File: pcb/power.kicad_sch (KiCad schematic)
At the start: 12 parts, among them U4 LP3993-33B3F

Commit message: Preliminary case design done, moving on to PCB design
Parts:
- removed TP1, TP2, TP3, TP4: ~, TestPoint:TestPoint_Pad_D2.0mm, symbol Connector:TestPoint
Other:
- note removed: "Test points"
- note removed: "label these on PCB"
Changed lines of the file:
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@@
-    (fill (type none))
-  )
-  (rectangle (start 25.4 60.96) (end 57.15 90.17)
-    (stroke (width 0) (type default))
     (fill (type none))
   )
@@
     (effects (font (size 1.5 1.5) (thickness 0.254) bold) (justify left bottom))
   )
-  (text "Test points" (at 26.67 64.77 0)
-    (effects (font (size 1.5 1.5) (thickness 0.254) bold) (justify left bottom))
-  )
   (text "3.3V stepdown" (at 76.2 29.21 0)
     (effects (font (size 1.5 1.5) (thickness 0.254) bold) (justify left bottom))
   )
-  (text "label these on PCB" (at 25.4 91.44 0)
-    (effects (font (size 0.7 0.7) italic (color 108 131 255 1)) (justify left bottom))
-  )
-  (symbol (lib_id "Connector:TestPoint") (at 33.02 72.39 180) (unit 1)
-    (in_bom yes) (on_board yes) (dnp no)
-    (property "Reference" "TP1" (at 27.94 71.12 0)
-      (effects (font (size 1.27 1.27)) (justify right))
-    )
-    (property "Value" "~" (at 21.59 73.66 0)
-      (effects (font (size 1.27 1.27)) (justify right))
-    )
-    (property "Footprint" "TestPoint:TestPoint_Pad_D2.0mm" (at 27.94 72.39 0)
-      (effects (font (size 1.27 1.27)) hide)
-    )
-    (property "Datasheet" "~" (at 27.94 72.39 0)
-      (effects (font (size 1.27 1.27)) hide)
-    )
-    (pin "1")
-    (instances
-      (project "keyboard"
-        (path "/fc529d87-72d0-4c92-b352-ddcf4c6f7199/55896886-29a1-46d7-b475-726a72adff13"
-          (reference "TP1") (unit 1)
-        )
-      )
-    )
-  )
   (symbol (lib_id "power:VBUS") (at 30.48 36.83 0) (unit 1)
     (in_bom yes) (on_board yes) (dnp no) (fields_autoplaced)
@@
     )
   )
-  (symbol (lib_id "power:+5V") (at 41.91 72.39 0) (unit 1)
-    (in_bom yes) (on_board yes) (dnp no) (fields_autoplaced)
-    (property "Reference" "#PWR03" (at 41.91 76.2 0)
-      (effects (font (size 1.27 1.27)) hide)
-    )
-    (property "Value" "+5V" (at 41.91 68.58 0)
-      (effects (font (size 1.27 1.27)))
-    )
-    (property "Footprint" "" (at 41.91 72.39 0)
-      (effects (font (size 1.27 1.27)) hide)
-    )
-    (property "Datasheet" "" (at 41.91 72.39 0)
-      (effects (font (size 1.27 1.27)) hide)
-    )
-    (pin "1")
-    (instances
-      (project "keyboard"
-        (path "/fc529d87-72d0-4c92-b352-ddcf4c6f7199/55896886-29a1-46d7-b475-726a72adff13"
-          (reference "#PWR03") (unit 1)
-        )
-      )
-    )
-  )
   (symbol (lib_name "GND_2") (lib_id "power:GND") (at 48.26 49.53 0) (unit 1)
     (in_bom yes) (on_board yes) (dnp no) (fields_autoplaced)
@@
         (path "/fc529d87-72d0-4c92-b352-ddcf4c6f7199/55896886-29a1-46d7-b475-726a72adff13"
           (reference "#PWR05") (unit 1)
-        )
-      )
-    )
-  )
-  (symbol (lib_id "Connector:TestPoint") (at 41.91 82.55 0) (unit 1)
-    (in_bom yes) (on_board yes) (dnp no)
-    (property "Reference" "TP3" (at 36.83 80.01 0)
-      (effects (font (size 1.27 1.27)) (justify left))
-    )
-    (property "Value" "~" (at 44.45 81.153 0)
-      (effects (font (size 1.27 1.27)) (justify left))
-    )
-    (property "Footprint" "TestPoint:TestPoint_Pad_D2.0mm" (at 46.99 82.55 0)
-      (effects (font (size 1.27 1.27)) hide)
-    )
-    (property "Datasheet" "~" (at 46.99 82.55 0)
-      (effects (font (size 1.27 1.27)) hide)
-    )
-    (pin "1")
-    (instances
-      (project "keyboard"
-        (path "/fc529d87-72d0-4c92-b352-ddcf4c6f7199/55896886-29a1-46d7-b475-726a72adff13"
-          (reference "TP3") (unit 1)
         )
       )
@@
     )
   )
-  (symbol (lib_id "power:+3.3V") (at 50.8 72.39 0) (unit 1)
-    (in_bom yes) (on_board yes) (dnp no) (fields_autoplaced)
-    (property "Reference" "#PWR06" (at 50.8 76.2 0)
-      (effects (font (size 1.27 1.27)) hide)
-    )
-    (property "Value" "+3.3V" (at 50.8 68.58 0)
-      (effects (font (size 1.27 1.27)))
-    )
-    (property "Footprint" "" (at 50.8 72.39 0)
-      (effects (font (size 1.27 1.27)) hide)
-    )
-    (property "Datasheet" "" (at 50.8 72.39 0)
-      (effects (font (size 1.27 1.27)) hide)
-    )
-    (pin "1")
-    (instances
-      (project "keyboard"
-        (path "/fc529d87-72d0-4c92-b352-ddcf4c6f7199/55896886-29a1-46d7-b475-726a72adff13"
-          (reference "#PWR06") (unit 1)
-        )
-      )
-    )
-  )
   (symbol (lib_id "Device:C_Small") (at 84.455 44.45 0) (mirror y) (unit 1)
     (in_bom yes) (on_board yes) (dnp no) (fields_autoplaced)
@@
     )
   )
-  (symbol (lib_id "power:VBUS") (at 33.02 72.39 0) (unit 1)
-    (in_bom yes) (on_board yes) (dnp no) (fields_autoplaced)
-    (property "Reference" "#PWR02" (at 33.02 76.2 0)
-      (effects (font (size 1.27 1.27)) hide)
-    )
-    (property "Value" "VBUS" (at 33.02 68.58 0)
-      (effects (font (size 1.27 1.27)))
-    )
-    (property "Footprint" "" (at 33.02 72.39 0)
-      (effects (font (size 1.27 1.27)) hide)
-    )
-    (property "Datasheet" "" (at 33.02 72.39 0)
-      (effects (font (size 1.27 1.27)) hide)
-    )
-    (pin "1")
-    (instances
-      (project "keyboard"
-        (path "/fc529d87-72d0-4c92-b352-ddcf4c6f7199/55896886-29a1-46d7-b475-726a72adff13"
-          (reference "#PWR02") (unit 1)
-        )
-      )
-    )
-  )
   (symbol (lib_id "Device:C") (at 48.26 43.18 0) (unit 1)
     (in_bom yes) (on_board yes) (dnp no) (fields_autoplaced)
@@
     )
   )
-  (symbol (lib_id "Connector:TestPoint") (at 41.91 72.39 180) (unit 1)
-    (in_bom yes) (on_board yes) (dnp no)
-    (property "Reference" "TP2" (at 36.83 71.12 0)
-      (effects (font (size 1.27 1.27)) (justify right))
-    )
-    (property "Value" "~" (at 44.45 73.66 0)
-      (effects (font (size 1.27 1.27)) (justify right))
-    )
-    (property "Footprint" "TestPoint:TestPoint_Pad_D2.0mm" (at 36.83 72.39 0)
-      (effects (font (size 1.27 1.27)) hide)
-    )
-    (property "Datasheet" "~" (at 36.83 72.39 0)
-      (effects (font (size 1.27 1.27)) hide)
-    )
-    (pin "1")
-    (instances
-      (project "keyboard"
-        (path "/fc529d87-72d0-4c92-b352-ddcf4c6f7199/55896886-29a1-46d7-b475-726a72adff13"
-          (reference "TP2") (unit 1)
-        )
-      )
-    )
-  )
   (symbol (lib_id "power:GND") (at 84.455 46.99 0) (mirror y) (unit 1)
     (in_bom yes) (on_board yes) (dnp no) (fields_autoplaced)
@@
     )
   )
-  (symbol (lib_id "Connector:TestPoint") (at 50.8 72.39 180) (unit 1)
-    (in_bom yes) (on_board yes) (dnp no)
-    (property "Reference" "TP4" (at 45.72 71.12 0)
-      (effects (font (size 1.27 1.27)) (justify right))
-    )
-    (property "Value" "~" (at 53.34 73.66 0)
-      (effects (font (size 1.27 1.27)) (justify right))
-    )
-    (property "Footprint" "TestPoint:TestPoint_Pad_D2.0mm" (at 45.72 72.39 0)
-      (effects (font (size 1.27 1.27)) hide)
-    )
-    (property "Datasheet" "~" (at 45.72 72.39 0)
-      (effects (font (size 1.27 1.27)) hide)
-    )
-    (pin "1")
-    (instances
-      (project "keyboard"
-        (path "/fc529d87-72d0-4c92-b352-ddcf4c6f7199/55896886-29a1-46d7-b475-726a72adff13"
-          (reference "TP4") (unit 1)
-        )
-      )
-    )
-  )
   (symbol (lib_id "Device:FerriteBead_Small") (at 43.18 38.1 90) (unit 1)
     (in_bom yes) (on_board yes) (dnp no) (fields_autoplaced)
@@
         )
       )
-    )
-  )
-  (symbol (lib_name "GND_1") (lib_id "power:GND") (at 41.91 82.55 0) (unit 1)
-    (in_bom yes) (on_board yes) (dnp no) (fields_autoplaced)
-    (property "Reference" "#PWR04" (at 41.91 88.9 0)
-      (effects (font (size 1.27 1.27)) hide)
-    )
-    (property "Value" "GND" (at 41.91 87.63 0)
-      (effects (font (size 1.27 1.27)))
-    )
-    (property "Footprint" "" (at 41.91 82.55 0)
-      (effects (font (size 1.27 1.27)) hide)
-    )
-    (property "Datasheet" "" (at 41.91 82.55 0)
-      (effects (font (size 1.27 1.27)) hide)
-    )
-    (pin "1")
-    (instances
-      (project "keyboard"
-        (path "/fc529d87-72d0-4c92-b352-ddcf4c6f7199/55896886-29a1-46d7-b475-726a72adff13"
-          (reference "#PWR04") (unit 1)
-        )
-      )

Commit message: PCB work in progress
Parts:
- removed C13, C16: 1u, Capacitor_SMD:C_0603_1608Metric, symbol Device:C_Small
- removed C3: 10u, Capacitor_SMD:C_0805_2012Metric, symbol Device:C
- removed C?: 100nF, Capacitor_SMD:C_0603_1608Metric, symbol Device:C_Small
- removed FB1: FerriteBead_Small, Inductor_SMD:L_0603_1608Metric, symbol Device:FerriteBead_Small
- removed U4: LP3993-33B3F, Package_TO_SOT_SMD:SOT-23, symbol AP2210N-3.3TRG1:AP2210N-3.3TRG1
- added U1: NCP1117-3.3_SOT223, Package_TO_SOT_SMD:SOT-223-3_TabPin2, symbol Regulator_Linear:NCP1117-3.3_SOT223
- C1: value 10n -> 10u; footprint Capacitor_SMD:C_0603_1608Metric -> Capacitor_SMD:C_0603_1608Metric_Pad1.08x0.95mm_HandSolder
- C2: value 100n -> 10u; footprint Capacitor_SMD:C_0603_1608Metric -> Capacitor_SMD:C_0603_1608Metric_Pad1.08x0.95mm_HandSolder
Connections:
- net +5V is gone; now on net VBUS: C2.1
- net GND: now also U1.1 (GND)
- net VBUS: now also U1.3 (VI); no longer C1.1
- new net +3V3: C1.1, U1.2 (VO)
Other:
- note removed: "3.3V stepdown"
- note removed: "VBUS Pi filter"

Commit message: Schematic done, starting PCB design
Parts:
- added D1: NCD0805O1, LED_SMD:LED_0805_2012Metric_Pad1.15x1.40mm_HandSolder, symbol Device:LED
- added R6 (x3): 27, Resistor_SMD:R_0603_1608Metric_Pad0.98x0.95mm_HandSolder, symbol Device:R
- renumbered C2 to C1, C1 to C2
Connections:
- net +3V3: now also R6.1
- net GND: now also D1.1 (K)
- new net: D1.2 (A), R6.2
- new net: R6.1, R6.2 (x2)
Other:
- note added: "Indicator LED"
- note added: "Linear regulator"
- note added: "Vf = ~2V Peak curr = 25mA Target curr = (3.3 - 2) / (27 + 27 + 27) = 16mA"
- moved on the sheet: C1, C2, U1

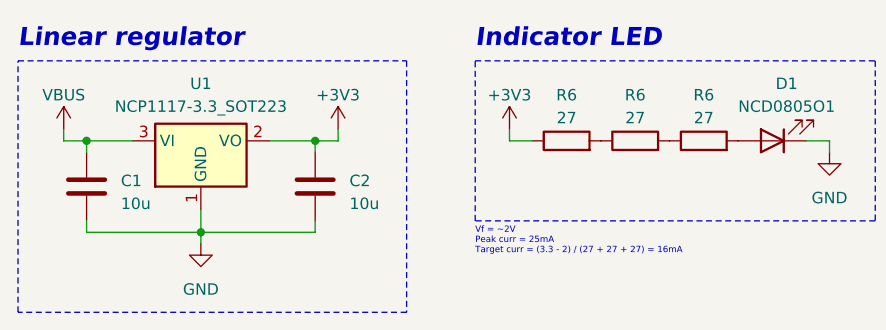
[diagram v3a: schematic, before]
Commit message: Rerouted a lot of stuff
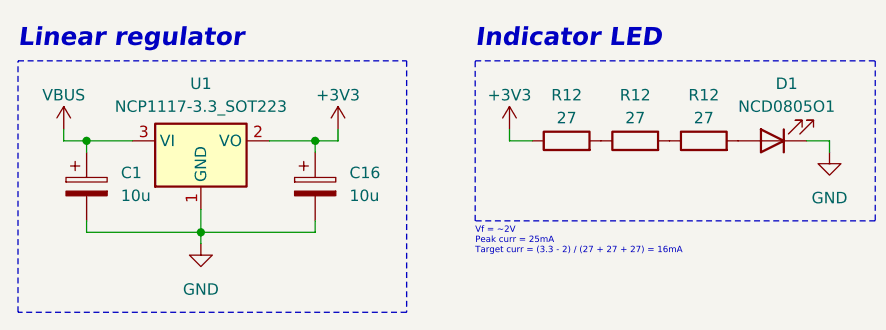
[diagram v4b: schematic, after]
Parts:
- removed C1, C2: 10u, Capacitor_SMD:C_0603_1608Metric_Pad1.08x0.95mm_HandSolder, symbol Device:C
- removed R6 (x3): 27, Resistor_SMD:R_0603_1608Metric_Pad0.98x0.95mm_HandSolder, symbol Device:R
- added C1, C16: 10u, Capacitor_SMD:C_1206_3216Metric, symbol Device:C_Polarized
- added R12 (x3): 27, Resistor_SMD:R_0402_1005Metric, symbol Device:R
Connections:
- net +3V3: now also C16.1, R12.1
- net GND: now also C1.2, C16.2
- net VBUS: now also C1.1
- net at D1.2 (A): now also R12.2
- new net: R12.1, R12.2 (x2)

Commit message: PCB design complete
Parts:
- C1, C16: LCSC (none) -> C7171
- D1: value NCD0805O1 -> NCD0805; LCSC (none) -> C84256
- R12: LCSC (none) -> C25100
- U1: LCSC (none) -> C26537
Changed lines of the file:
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@@
+      (effects (font (size 1.27 1.27)) hide)
+    )
+    (property "LCSC" "C7171" (at 116.84 87.63 0)
       (effects (font (size 1.27 1.27)) hide)
     )
@@
       (effects (font (size 1.27 1.27)) hide)
     )
+    (property "LCSC" "C7171" (at 91.44 87.63 0)
+      (effects (font (size 1.27 1.27)) hide)
+    )
     (pin "1")
     (pin "2")
@@
       (effects (font (size 1.27 1.27)))
     )
-    (property "Value" "NCD0805O1" (at 169.2275 78.74 0)
+    (property "Value" "NCD0805" (at 169.2275 78.74 0)
       (effects (font (size 1.27 1.27)))
     )
@@
       (effects (font (size 1.27 1.27)) hide)
     )
+    (property "LCSC" "C84256" (at 167.64 82.55 0)
+      (effects (font (size 1.27 1.27)) hide)
+    )
     (pin "1")
     (pin "2")
@@
     )
     (property "Datasheet" "~" (at 144.78 82.55 0)
+      (effects (font (size 1.27 1.27)) hide)
+    )
+    (property "LCSC" "C25100" (at 144.78 82.55 90)
       (effects (font (size 1.27 1.27)) hide)
     )
@@
       (effects (font (size 1.27 1.27)) hide)
     )
+    (property "LCSC" "C25100" (at 152.4 82.55 90)
+      (effects (font (size 1.27 1.27)) hide)
+    )
     (pin "1")
     (pin "2")
@@
       (effects (font (size 1.27 1.27)) hide)
     )
+    (property "LCSC" "C26537" (at 104.14 82.55 0)
+      (effects (font (size 1.27 1.27)) hide)
+    )
     (pin "1")
     (pin "2")
@@
       (effects (font (size 1.27 1.27)) hide)
     )
+    (property "LCSC" "C25100" (at 160.02 82.55 90)
+      (effects (font (size 1.27 1.27)) hide)
+    )
